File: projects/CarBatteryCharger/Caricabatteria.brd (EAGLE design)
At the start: 50.5 x 61 mm, 22 parts, among them T1 TAG 665-100, X1 MKDSN1,5/2-5,08, X2 MKDSN1,5/2-5,08, X3 MKDSN1,5/2-5,08

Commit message: Some detail adjust.
Some detail adjust.
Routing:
- net N$11: track 104.4 -> 98.3 mm
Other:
- board text added: "2020-03-18"
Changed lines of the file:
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@@
 <drawing>
 <settings>
-<setting alwaysvectorfont="no"/>
+<setting alwaysvectorfont="yes"/>
 <setting verticaltext="up"/>
 </settings>
@@
 <text x="40.64" y="57.15" size="2.1844" layer="16" font="vector" ratio="15" rot="MR0">IZØVLL-CARBATT</text>
 <text x="13.97" y="55.88" size="2.54" layer="16" font="vector" ratio="15" rot="MR0">V.1</text>
+<text x="41.91" y="1.27" size="2" layer="16" rot="MR0">2020-03-18</text>
 </plain>
 <attributes>
@@
 <wire x1="30.48" y1="11.43" x2="26.67" y2="15.24" width="1.27" layer="16"/>
 <wire x1="25.4" y1="15.24" x2="26.67" y2="15.24" width="1.27" layer="16"/>
-<wire x1="30.48" y1="11.43" x2="30.48" y2="3.81" width="1.27" layer="16"/>
-<wire x1="30.48" y1="3.81" x2="31.75" y2="2.54" width="1.27" layer="16"/>
-<wire x1="31.75" y1="2.54" x2="39.37" y2="2.54" width="1.27" layer="16"/>
-<wire x1="39.37" y1="2.54" x2="48.819" y2="11.989" width="1.27" layer="16"/>
+<wire x1="30.48" y1="11.43" x2="30.48" y2="8.89" width="1.27" layer="16"/>
+<wire x1="30.48" y1="8.89" x2="33.02" y2="6.35" width="1.27" layer="16"/>
+<wire x1="33.02" y1="6.35" x2="43.18" y2="6.35" width="1.27" layer="16"/>
+<wire x1="43.18" y1="6.35" x2="48.819" y2="11.989" width="1.27" layer="16"/>
 <wire x1="48.819" y1="50.241" x2="46.99" y2="52.07" width="1.27" layer="16"/>
 <wire x1="48.819" y1="11.989" x2="48.819" y2="24.13" width="1.27" layer="16"/>

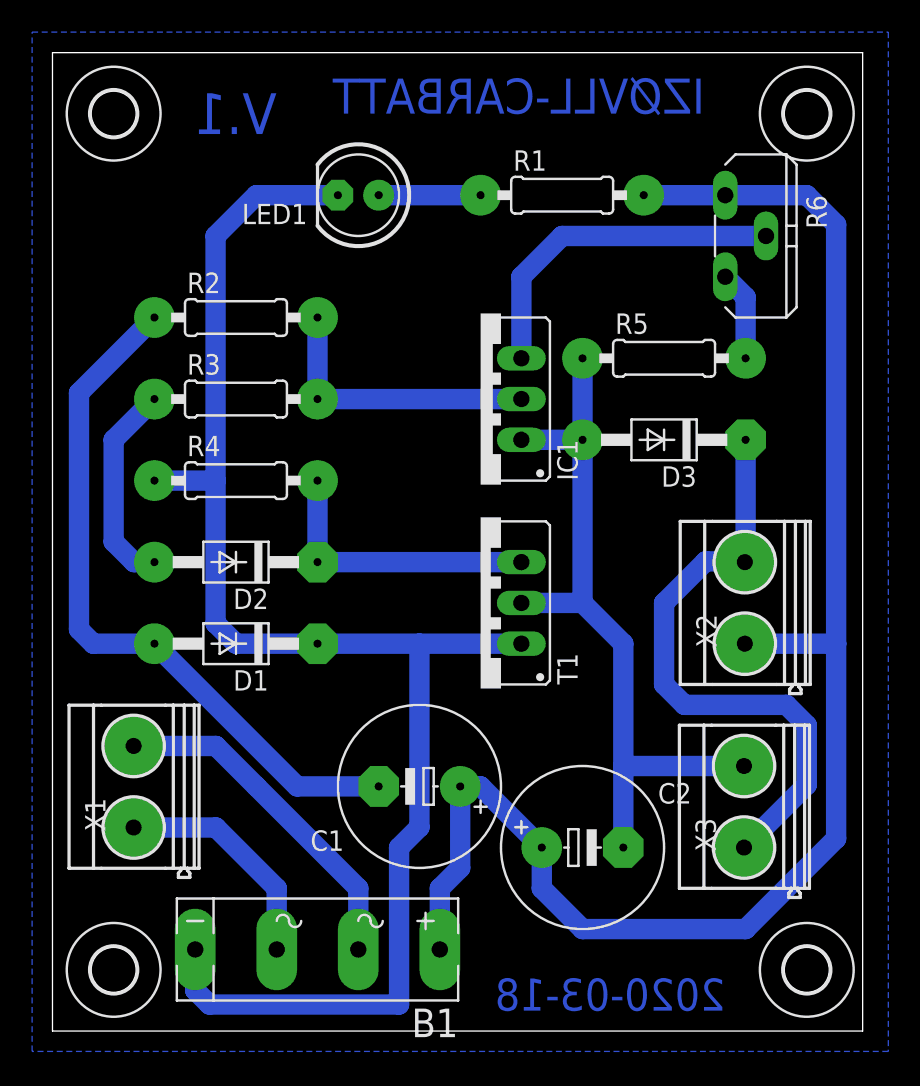
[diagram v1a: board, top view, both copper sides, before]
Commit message: Correct value of some component
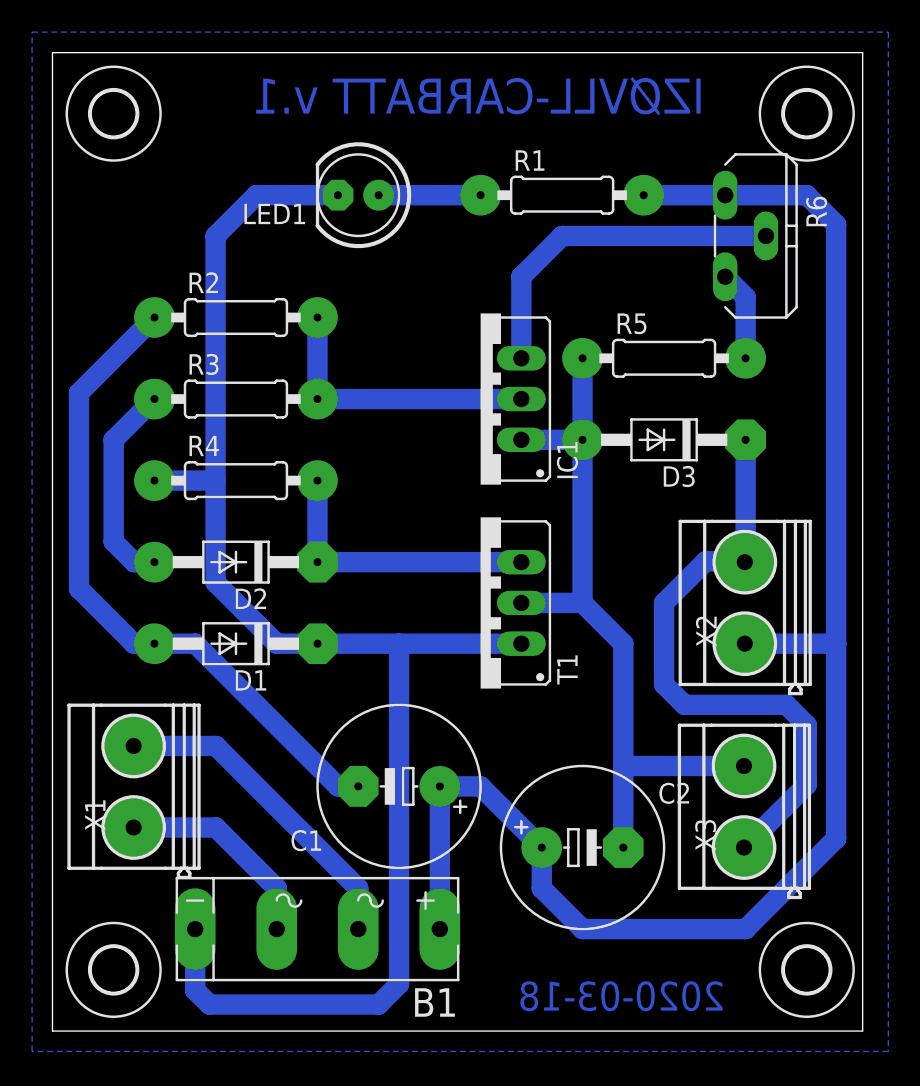
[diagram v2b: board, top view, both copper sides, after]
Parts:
- B1: value (none) -> 5A
- IC1: value (none) -> 7912
- LED1: value (none) -> RED 5MM
- R6: value (none) -> 1K
- moved B1 1.27 mm to (16.5, 6.35)
- moved C1 1.27 mm to (21.6, 15.2)
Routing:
- net N$1: track 44.1 -> 41.3 mm
- net N$7: track 94.8 -> 93.3 mm
- net N$13: track 14.3 -> 13.0 mm
- net N$12: track 21.5 -> 20.2 mm
- net N$11: track 98.3 -> 97.8 mm
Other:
- board text added: "IZØVLL-CARBATT v.1"
- board text removed: "IZØVLL-CARBATT"
- board text removed: "V.1"
